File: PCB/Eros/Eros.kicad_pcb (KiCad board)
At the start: 4 copper layers, 65 x 71 mm, 117 parts, among them IC1 ADS1292RIPBS, J1 USB_C_PowerOnly_6P, J2 UART, J3 Li-ion, J4 Conn_01x08_Socket, J5 AudioJack3, J6 Micro_SD_Card, J7 Conn_01x03_Socket, Q1 BC817, SW1 SW_Push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

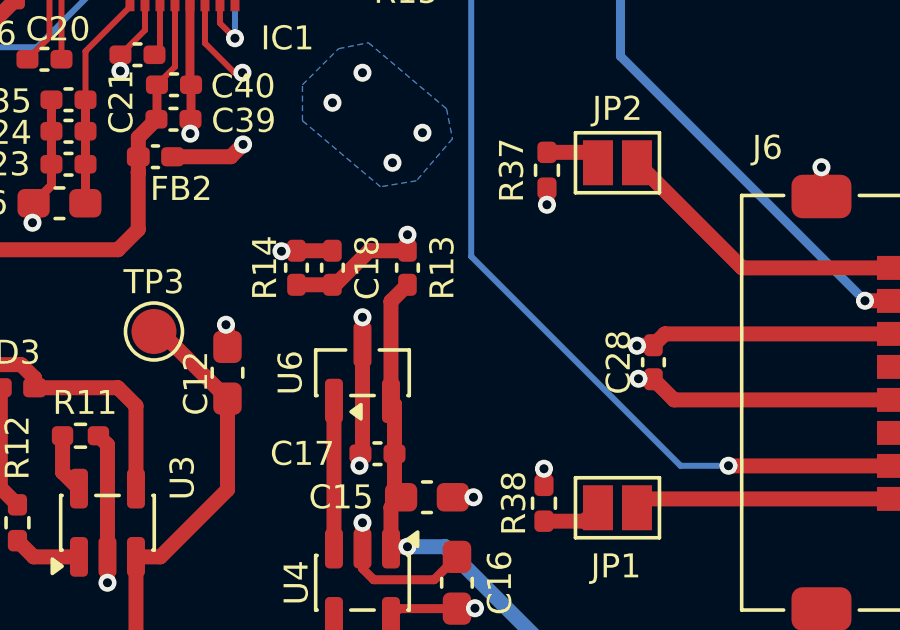
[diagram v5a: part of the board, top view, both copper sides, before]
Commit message: update Q1 with library, change R13/R14 from C to R, change R18/R20 to 45k, change c28 to 0603 size
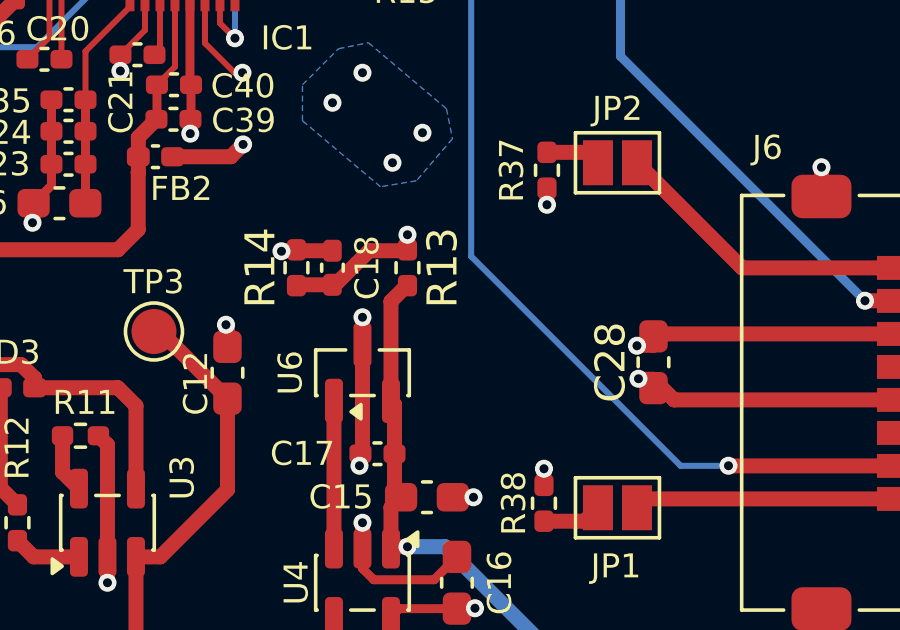
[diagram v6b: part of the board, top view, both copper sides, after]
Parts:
- C28: footprint Capacitor_SMD:C_0402_1005Metric_Pad0.74x0.62mm_HandSolder -> Capacitor_SMD:C_0603_1608Metric_Pad1.08x0.95mm_HandSolder
- R13, R14: footprint Capacitor_SMD:C_0402_1005Metric_Pad0.74x0.62mm_HandSolder -> Resistor_SMD:R_0402_1005Metric_Pad0.72x0.64mm_HandSolder
- R18, R20: value 40.2k -> 45k
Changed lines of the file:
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@@
 		)
 	)
-	(footprint "Capacitor_SMD:C_0402_1005Metric_Pad0.74x0.62mm_HandSolder"
+	(footprint "Capacitor_SMD:C_0603_1608Metric_Pad1.08x0.95mm_HandSolder"
 		(layer "F.Cu")
 		(at 199.7 102.65 90)
-		(descr "Capacitor SMD 0402 (1005 Metric), square (rectangular) end terminal, IPC-7351 nominal with elongated pad for handsoldering. (Body size source: IPC-SM-782 page 76, https://www.pcb-3d.com/wordpress/wp-content/uploads/ipc-sm-782a_amendment_1_and_2.pdf), generated with kicad-footprint-generator")
+		(descr "Capacitor SMD 0603 (1608 Metric), square (rectangular) end terminal, IPC-7351 nominal with elongated pad for handsoldering. (Body size source: IPC-SM-782 page 76, https://www.pcb-3d.com/wordpress/wp-content/uploads/ipc-sm-782a_amendment_1_and_2.pdf), generated with kicad-footprint-generator")
 		(tags "capacitor handsolder")
 		(property "Reference" "C28"
-			(at 0 -1.16 90)
+			(at 0 -1.43 90)
 			(layer "F.SilkS")
 			(effects
 				(font
-					(size 0.8 0.8)
+					(size 1 1)
 					(thickness 0.15)
 				)
@@
 		)
 		(property "Value" "10u"
-			(at 0 1.16 90)
+			(at 0 1.43 90)
 			(layer "F.Fab")
 			(effects
@@
 		(attr smd)
 		(fp_line
-			(start -0.115835 -0.36)
-			(end 0.115835 -0.36)
+			(start -0.146267 -0.51)
+			(end 0.146267 -0.51)
 			(stroke
 				(width 0.12)
@@
 		)
 		(fp_line
-			(start -0.115835 0.36)
-			(end 0.115835 0.36)
+			(start -0.146267 0.51)
+			(end 0.146267 0.51)
 			(stroke
 				(width 0.12)
@@
 		)
 		(fp_rect
-			(start -1.09 -0.46)
-			(end 1.09 0.46)
+			(start -1.65 -0.73)
+			(end 1.65 0.73)
 			(stroke
 				(width 0.05)
@@
 		)
 		(fp_rect
-			(start -0.5 -0.25)
-			(end 0.5 0.25)
+			(start -0.8 -0.4)
+			(end 0.8 0.4)
 			(stroke
 				(width 0.1)
@@
 			(effects
 				(font
-					(size 0.25 0.25)
-					(thickness 0.04)
+					(size 0.4 0.4)
+					(thickness 0.06)
 				)
 			)
 		)
 		(pad "1" smd roundrect
-			(at -0.5675 0 90)
-			(size 0.735 0.62)
+			(at -0.8625 0 90)
+			(size 1.075 0.95)
 			(layers "F.Cu" "F.Mask" "F.Paste")
 			(roundrect_rratio 0.25)
@@
 		)
 		(pad "2" smd roundrect
-			(at 0.5675 0 90)
-			(size 0.735 0.62)
+			(at 0.8625 0 90)
+			(size 1.075 0.95)
 			(layers "F.Cu" "F.Mask" "F.Paste")
 			(roundrect_rratio 0.25)
@@
 		)
 		(embedded_fonts no)
-		(model "${KICAD9_3DMODEL_DIR}/Capacitor_SMD.3dshapes/C_0402_1005Metric.step"
+		(model "${KICAD9_3DMODEL_DIR}/Capacitor_SMD.3dshapes/C_0603_1608Metric.step"
 			(offset
 				(xyz 0 0 0)
@@
 			)
 		)
-		(property "Value" "40.2k"
+		(property "Value" "45k"
 			(at 0 1.17 0)
 			(layer "F.Fab")
@@
 			)
 		)
-		(property "Value" "40.2k"
+		(property "Value" "45k"
 			(at 0 1.17 0)
 			(layer "F.Fab")
@@
 		)
 	)
-	(footprint "Capacitor_SMD:C_0402_1005Metric_Pad0.74x0.62mm_HandSolder"
+	(footprint "Resistor_SMD:R_0402_1005Metric_Pad0.72x0.64mm_HandSolder"
 		(layer "F.Cu")
 		(at 187.8 99.5 -90)
-		(descr "Capacitor SMD 0402 (1005 Metric), square (rectangular) end terminal, IPC-7351 nominal with elongated pad for handsoldering. (Body size source: IPC-SM-782 page 76, https://www.pcb-3d.com/wordpress/wp-content/uploads/ipc-sm-782a_amendment_1_and_2.pdf), generated with kicad-footprint-generator")
-		(tags "capacitor handsolder")
+		(descr "Resistor SMD 0402 (1005 Metric), square (rectangular) end terminal, IPC-7351 nominal with elongated pad for handsoldering. (Body size source: IPC-SM-782 page 72, https://www.pcb-3d.com/wordpress/wp-content/uploads/ipc-sm-782a_amendment_1_and_2.pdf), generated with kicad-footprint-generator")
+		(tags "resistor handsolder")
 		(property "Reference" "R14"
-			(at 0 1.05 90)
+			(at 0 1.2 270)
 			(layer "F.SilkS")
 			(effects
 				(font
-					(size 0.8 0.8)
+					(size 1 1)
 					(thickness 0.15)
 				)
@@
 		)
 		(property "Value" "1M"
-			(at 0 1.16 90)
+			(at 0 1.17 270)
 			(layer "F.Fab")
 			(effects
@@
 		)
 		(property "Datasheet" "~"
-			(at 0 0 90)
+			(at 0 0 270)
 			(layer "F.Fab")
 			(hide yes)
@@
 		)
 		(property "Description" "Resistor"
-			(at 0 0 90)
+			(at 0 0 270)
 			(layer "F.Fab")
 			(hide yes)
@@
 		(attr smd)
 		(fp_line
-			(start -0.115835 0.36)
-			(end 0.115835 0.36)
+			(start -0.167621 0.38)
+			(end 0.167621 0.38)
 			(stroke
 				(width 0.12)
@@
 		)
 		(fp_line
-			(start -0.115835 -0.36)
-			(end 0.115835 -0.36)
+			(start -0.167621 -0.38)
+			(end 0.167621 -0.38)
 			(stroke
 				(width 0.12)
@@
 		)
 		(fp_rect
-			(start -1.09 -0.46)
-			(end 1.09 0.46)
+			(start -1.11 -0.47)
+			(end 1.11 0.47)
 			(stroke
 				(width 0.05)
@@
 		)
 		(fp_rect
-			(start -0.5 -0.25)
-			(end 0.5 0.25)
+			(start -0.525 -0.27)
+			(end 0.525 0.27)
 			(stroke
 				(width 0.1)
@@
 		)
 		(fp_text user "${REFERENCE}"
-			(at 0 0 90)
+			(at 0 0 270)
 			(layer "F.Fab")
 			(effects
 				(font
-					(size 0.25 0.25)
+					(size 0.26 0.26)
 					(thickness 0.04)
 				)
@@
 		)
 		(pad "1" smd roundrect
-			(at -0.5675 0 270)
-			(size 0.735 0.62)
+			(at -0.5975 0 270)
+			(size 0.715 0.64)
 			(layers "F.Cu" "F.Mask" "F.Paste")
 			(roundrect_rratio 0.25)
@@
 		)
 		(pad "2" smd roundrect
-			(at 0.5675 0 270)
-			(size 0.735 0.62)
+			(at 0.5975 0 270)
+			(size 0.715 0.64)
 			(layers "F.Cu" "F.Mask" "F.Paste")
 			(roundrect_rratio 0.25)
@@
 		)
 		(embedded_fonts no)
-		(model "${KICAD9_3DMODEL_DIR}/Capacitor_SMD.3dshapes/C_0402_1005Metric.step"
+		(model "${KICAD9_3DMODEL_DIR}/Resistor_SMD.3dshapes/R_0402_1005Metric.step"
 			(offset
 				(xyz 0 0 0)
@@
 		(embedded_fonts no)
 	)
-	(footprint "Capacitor_SMD:C_0402_1005Metric_Pad0.74x0.62mm_HandSolder"
+	(footprint "Resistor_SMD:R_0402_1005Metric_Pad0.72x0.64mm_HandSolder"
 		(layer "F.Cu")
 		(at 191.5 99.5 -90)
-		(descr "Capacitor SMD 0402 (1005 Metric), square (rectangular) end terminal, IPC-7351 nominal with elongated pad for handsoldering. (Body size source: IPC-SM-782 page 76, https://www.pcb-3d.com/wordpress/wp-content/uploads/ipc-sm-782a_amendment_1_and_2.pdf), generated with kicad-footprint-generator")
-		(tags "capacitor handsolder")
+		(descr "Resistor SMD 0402 (1005 Metric), square (rectangular) end terminal, IPC-7351 nominal with elongated pad for handsoldering. (Body size source: IPC-SM-782 page 72, https://www.pcb-3d.com/wordpress/wp-content/uploads/ipc-sm-782a_amendment_1_and_2.pdf), generated with kicad-footprint-generator")
+		(tags "resistor handsolder")
 		(property "Reference" "R13"
-			(at 0 -1.16 90)
+			(at 0 -1.17 270)
 			(layer "F.SilkS")
 			(effects
 				(font
-					(size 0.8 0.8)
+					(size 1 1)
 					(thickness 0.15)
 				)
@@
 		)
 		(property "Value" "1M"
-			(at 0 1.16 90)
+			(at 0 1.17 270)
 			(layer "F.Fab")
 			(effects
@@
 		)
 		(property "Datasheet" "~"
-			(at 0 0 90)
+			(at 0 0 270)
 			(layer "F.Fab")
 			(hide yes)
@@
 		)
 		(property "Description" "Resistor"
-			(at 0 0 90)
+			(at 0 0 270)
 			(layer "F.Fab")
 			(hide yes)
@@
 		(attr smd)
 		(fp_line
-			(start -0.115835 0.36)
-			(end 0.115835 0.36)
+			(start -0.167621 0.38)
+			(end 0.167621 0.38)
 			(stroke
 				(width 0.12)
@@
 		)
 		(fp_line
-			(start -0.115835 -0.36)
-			(end 0.115835 -0.36)
+			(start -0.167621 -0.38)
+			(end 0.167621 -0.38)
 			(stroke
 				(width 0.12)
@@
 		)
 		(fp_rect
-			(start -1.09 -0.46)
-			(end 1.09 0.46)
+			(start -1.11 -0.47)
+			(end 1.11 0.47)
 			(stroke
 				(width 0.05)
@@
 		)
 		(fp_rect
-			(start -0.5 -0.25)
-			(end 0.5 0.25)
+			(start -0.525 -0.27)
+			(end 0.525 0.27)
 			(stroke
 				(width 0.1)
@@
 		)
 		(fp_text user "${REFERENCE}"
-			(at 0 0 90)
+			(at 0 0 270)
 			(layer "F.Fab")
 			(effects
 				(font
-					(size 0.25 0.25)
+					(size 0.26 0.26)
 					(thickness 0.04)
 				)
@@
 		)
 		(pad "1" smd roundrect
-			(at -0.5675 0 270)
-			(size 0.735 0.62)
+			(at -0.5975 0 270)
+			(size 0.715 0.64)
 			(layers "F.Cu" "F.Mask" "F.Paste")
 			(roundrect_rratio 0.25)
@@
 		)
 		(pad "2" smd roundrect
-			(at 0.5675 0 270)
-			(size 0.735 0.62)
+			(at 0.5975 0 270)
+			(size 0.715 0.64)
 			(layers "F.Cu" "F.Mask" "F.Paste")
 			(roundrect_rratio 0.25)
@@
 		)
 		(embedded_fonts no)
-		(model "${KICAD9_3DMODEL_DIR}/Capacitor_SMD.3dshapes/C_0402_1005Metric.step"
+		(model "${KICAD9_3DMODEL_DIR}/Resistor_SMD.3dshapes/R_0402_1005Metric.step"
 			(offset
 				(xyz 0 0 0)
@@
 					(thickness 0.15)
 				)
+			)
+		)
+		(property "Sim.Device" "NPN"
+			(at 0 0 270)
+			(unlocked yes)
+			(layer "F.Fab")
+			(hide yes)
+			(effects
+				(font
+					(size 1 1)
+					(thickness 0.15)
+				)
+			)
+		)
+		(property "Sim.Pins" "1=B 2=E 3=C"
+			(at 0 0 270)
+			(unlocked yes)
+			(layer "F.Fab")
+			(hide yes)
+			(effects
+				(font
+					(size 1 1)
+					(thickness 0.15)
+				)

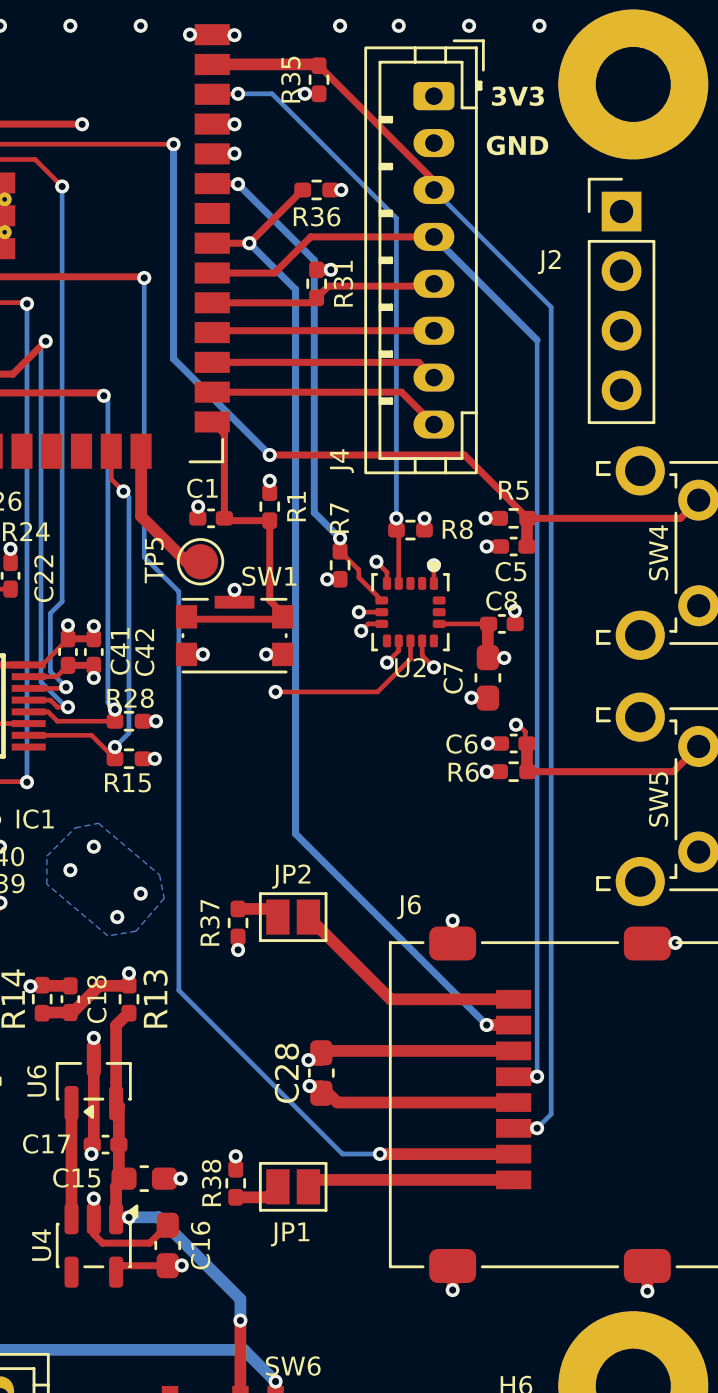
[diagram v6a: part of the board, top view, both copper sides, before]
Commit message: Flip SD card orientation
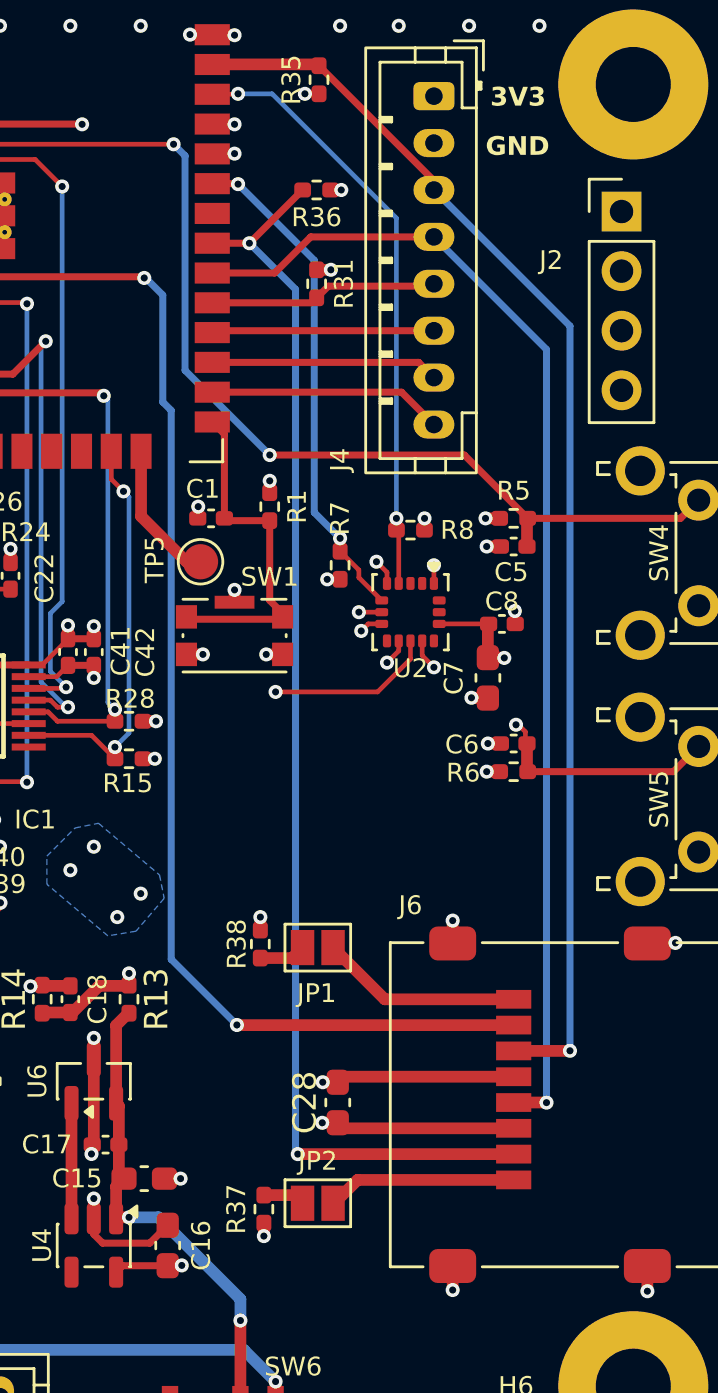
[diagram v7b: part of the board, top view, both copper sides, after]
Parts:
- moved R37 12.2 mm to (197.2, 108.5)
- moved JP2 12.2 mm to (199.6, 108.2)
- moved JP1 10.3 mm to (199.6, 97.3)
- moved R38 10.3 mm to (197.1, 97.2)
- moved C28 1.44 mm to (200.4, 103.9), turned to -90 degrees
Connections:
- J6 pad 1: Net-(J6-DAT2) -> Net-(J6-DAT1)
- J6 pad 2: MICRO_SD_CS -> VSPI_MISO
- J6 pad 3: VSPI_MOSI -> GND
- J6 pad 4: +3.3V -> VSPI_SCK
- J6 pad 5: VSPI_SCK -> +3.3V
- J6 pad 6: GND -> VSPI_MOSI
- J6 pad 7: VSPI_MISO -> MICRO_SD_CS
- J6 pad 8: Net-(J6-DAT1) -> Net-(J6-DAT2)
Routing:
- net VSPI_MISO: track 43.5 -> 53.7 mm
- net MICRO_SD_CS: track 65.9 -> 63.1 mm
- net Net-(J6-DAT1): track 10.2 -> 8.06 mm
- net VSPI_MOSI: track 55.1 -> 53.3 mm
- net VSPI_SCK: track 48.7 -> 50.4 mm
- net +3.3V: track 57.0 -> 56.2 mm
- net GND: track 90.3 -> 89.7 mm
